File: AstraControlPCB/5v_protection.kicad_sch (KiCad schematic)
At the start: 9 parts, among them U2 NCP361SNT1G

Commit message: Updates
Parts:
- renumbered R14 to R8, R8 to R9
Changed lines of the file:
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@@
 			)
 		)
-		(property "Datasheet" ""
+		(property "Datasheet" "https://www.lcsc.com/product-detail/Thimble-Copper-Rod-Test-Ring_ronghe-RH-5000_C5277086.html"
 			(at 177.8 119.38 90)
 			(effects
@@
 		(dnp no)
 		(fields_autoplaced yes)
-		(property "Reference" "R14"
+		(property "Reference" "R8"
 			(at 116.84 100.33 0)
 			(effects
@@
 			(project "AstraControl"
 				(path "/9a751838-dce8-4d69-8a02-736625ac74e7/0db21d8e-3390-4d67-877f-0e5d98e37848/e21714b4-6921-40f8-8882-480f43314016"
-					(reference "R14")
+					(reference "R8")
 					(unit 1)
 				)
@@
 		(dnp no)
 		(fields_autoplaced yes)
-		(property "Reference" "R8"
+		(property "Reference" "R9"
 			(at 241.3 90.17 0)
 			(effects
@@
 			(project "AstraControl"
 				(path "/9a751838-dce8-4d69-8a02-736625ac74e7/0db21d8e-3390-4d67-877f-0e5d98e37848/e21714b4-6921-40f8-8882-480f43314016"
-					(reference "R8")
+					(reference "R9")
 					(unit 1)
 				)
@@
 			)
 		)
-		(property "Datasheet" ""
+		(property "Datasheet" "https://www.lcsc.com/product-detail/Thimble-Copper-Rod-Test-Ring_ronghe-RH-5000_C5277086.html"
 			(at 114.3 76.2 90)
 			(effects

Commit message: Added MFN MPR to each components for eurocircuits
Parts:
- C7, C8: MFN (none) -> Samsung Electro-Mechanics; MPR (none) -> CL05A105KA5NQNC
- LED2: MFN (none) -> Hubei KENTO Elec; MPN (none) -> KT-0603R
- R8: MFN (none) -> UNI-ROYAL(Uniroyal Elec); MPN (none) -> 0805W8F1004T5E
- R9: MFN (none) -> UNI-ROYAL(Uniroyal Elec); MPN (none) -> 0402WGF2200TCE
- TP5, TP6: MFN (none) -> ronghe; MPN (none) -> RH-5000
- U2: MFN (none) -> onsemi; MPN (none) -> NCP361SNT1G
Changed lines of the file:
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@@
 			)
 		)
-		(property "Description" "Multilayer Ceramic Capacitor"
+		(property "Description" "25V 1uF X5R ±10% 0402 Multilayer Ceramic Capacitors MLCC - SMD/SMT ROHS"
 			(at 132.08 91.44 0)
 			(effects
@@
 				)
 				(justify right)
+			)
+		)
+		(property "MFN" "Samsung Electro-Mechanics"
+			(at 151.13 91.44 0)
+			(effects
+				(font
+					(size 1.27 1.27)
+				)
+				(hide yes)
+			)
+		)
+		(property "MPR" "CL05A105KA5NQNC"
+			(at 147.32 91.44 0)
+			(effects
+				(font
+					(size 1.27 1.27)
+				)
+				(hide yes)
 			)
 		)
@@
 			)
 		)
-		(property "Description" "0603 Smd LED Emitting Color Red"
+		(property "Description" "-40℃~+85℃ Red 0603 LED Indication - Discrete ROHS"
 			(at 208.28 104.14 0)
 			(effects
@@
 					(bold yes)
 				)
+			)
+		)
+		(property "MFN" "Hubei KENTO Elec"
+			(at 208.28 123.19 0)
+			(effects
+				(font
+					(size 1.27 1.27)
+				)
+				(hide yes)
+			)
+		)
+		(property "MPN" "KT-0603R"
+			(at 208.28 123.19 0)
+			(effects
+				(font
+					(size 1.27 1.27)
+				)
+				(hide yes)
 			)
 		)
@@
 			)
 		)
-		(property "Description" ""
+		(property "Description" "Test Points / Test Rings ROHS"
 			(at 177.8 119.38 90)
 			(effects
@@
 				)
 				(justify left)
+			)
+		)
+		(property "MFN" "ronghe"
+			(at 177.8 153.67 0)
+			(effects
+				(font
+					(size 1.27 1.27)
+				)
+				(hide yes)
+			)
+		)
+		(property "MPN" "RH-5000"
+			(at 177.8 153.67 0)
+			(effects
+				(font
+					(size 1.27 1.27)
+				)
+				(hide yes)
 			)
 		)
@@
 			)
 		)
-		(property "Description" "Chip Resistor - Surface Mount ROHS"
+		(property "Description" "125mW Thick Film Resistors 150V ±100ppm/℃ ±1% 1MΩ 0805 Chip Resistor - Surface Mount ROHS"
 			(at 116.84 104.14 0)
 			(effects
@@
 					(bold yes)
 				)
+			)
+		)
+		(property "MFN" "UNI-ROYAL(Uniroyal Elec)"
+			(at 116.84 88.9 0)
+			(effects
+				(font
+					(size 1.27 1.27)
+				)
+				(hide yes)
+			)
+		)
+		(property "MPN" "0805W8F1004T5E"
+			(at 116.84 88.9 0)
+			(effects
+				(font
+					(size 1.27 1.27)
+				)
+				(hide yes)
 			)
 		)
@@
 			)
 		)
-		(property "Description" "Thick Film Resistors"
+		(property "Description" "62.5mW Thick Film Resistors 50V ±100ppm/℃ ±1% 220Ω 0402 Chip Resistor - Surface Mount ROHS"
 			(at 241.3 93.98 0)
 			(effects
@@
 					(bold yes)
 				)
+			)
+		)
+		(property "MFN" "UNI-ROYAL(Uniroyal Elec)"
+			(at 241.3 78.74 0)
+			(effects
+				(font
+					(size 1.27 1.27)
+				)
+				(hide yes)
+			)
+		)
+		(property "MPN" "0402WGF2200TCE"
+			(at 241.3 78.74 0)
+			(effects
+				(font
+					(size 1.27 1.27)
+				)
+				(hide yes)
 			)
 		)
@@
 			)
 		)
+		(property "MFN" "onsemi"
+			(at 152.4 157.48 0)
+			(effects
+				(font
+					(size 1.27 1.27)
+				)
+				(hide yes)
+			)
+		)
+		(property "MPN" "NCP361SNT1G"
+			(at 152.4 157.48 0)
+			(effects
+				(font
+					(size 1.27 1.27)
+				)
+				(hide yes)
+			)
+		)
 		(pin "2"
 		)
@@
 			)
 		)
-		(property "Description" "Multilayer Ceramic Capacitor"
+		(property "Description" "25V 1uF X5R ±10% 0402 Multilayer Ceramic Capacitors MLCC - SMD/SMT ROHS"
 			(at 165.1 91.44 0)
 			(effects
@@
 				)
 				(justify left)
+			)
+		)
+		(property "MFN" "Samsung Electro-Mechanics"
+			(at 146.05 91.44 0)
+			(effects
+				(font
+					(size 1.27 1.27)
+				)
+				(hide yes)
+			)
+		)
+		(property "MPR" "CL05A105KA5NQNC"
+			(at 149.86 91.44 0)
+			(effects
+				(font
+					(size 1.27 1.27)
+				)
+				(hide yes)
 			)
 		)
@@
 			)
 		)
-		(property "Description" ""
+		(property "Description" "Test Points / Test Rings ROHS"
 			(at 114.3 76.2 90)
 			(effects
@@
 			)
 		)
+		(property "MFN" "ronghe"
+			(at 114.3 110.49 0)
+			(effects
+				(font
+					(size 1.27 1.27)
+				)
+				(hide yes)
+			)
+		)
+		(property "MPN" "RH-5000"
+			(at 114.3 110.49 0)
+			(effects
+				(font
+					(size 1.27 1.27)
+				)
+				(hide yes)
+			)
+		)

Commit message: Migrate library to submodule
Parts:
- C7, C8: MPN (none) -> CL05A105KA5NQNC
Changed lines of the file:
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@@
+			)
+		)
+		(property "MPN" "CL05A105KA5NQNC"
+			(at 147.32 91.44 0)
+			(effects
+				(font
+					(size 1.27 1.27)
+				)
+				(hide yes)
 			)
 		)
@@
 			(at 149.86 91.44 0)
 			(effects
+				(font
+					(size 1.27 1.27)
+				)
+				(hide yes)
+			)
+		)
+		(property "MPN" "CL05A105KA5NQNC"
+			(at 149.86 91.44 0)
+			(effects

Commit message: Update schematic titles, templates
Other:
- title: AstraControl - Root -> AstraControl - 5V Protection
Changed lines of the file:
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@@
 	(paper "A4")
 	(title_block
-		(title "AstraControl - Root")
+		(title "AstraControl - 5V Protection")
 		(date "2024-08-26")
 		(rev "A")

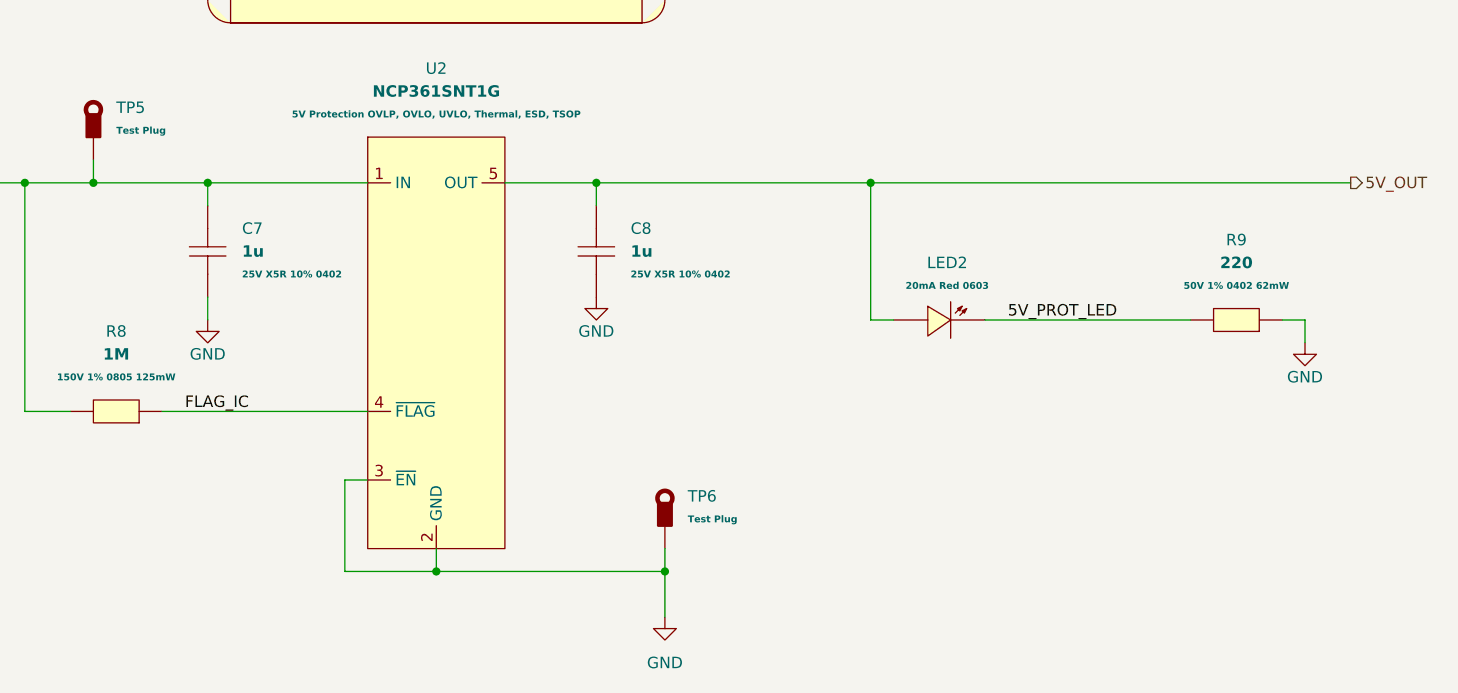
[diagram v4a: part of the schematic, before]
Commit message: Update to new rs485 chip, use 2 bit 5v gpio
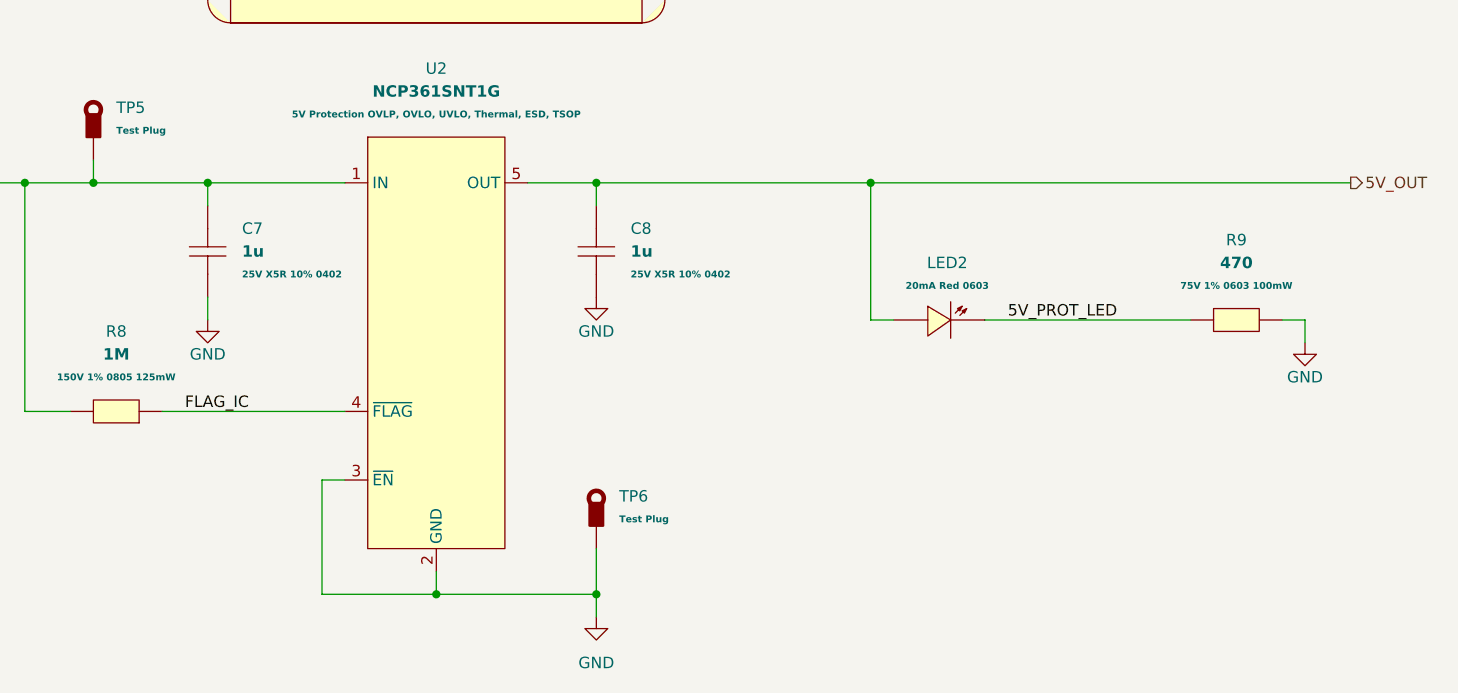
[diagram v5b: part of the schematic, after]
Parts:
- removed R9: 220, LiveAstra:R_0402_1005Metric, symbol LiveAstra:R_220Ohm_0402_62mW
- added R9: 470, LiveAstra:R_0603_1608Metric, symbol LiveAstra:R_470Ohm_0603_100mW
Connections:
- net 5V_PROT_LED: now also R9.1
- net GND: now also R9.2
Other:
- moved on the sheet: TP6, U2

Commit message: New inductor that is in stock, updated rs485 ic layout to put caps closer
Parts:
- renumbered INF3 to INF4, R9 to R10, R8 to R9
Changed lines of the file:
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@@
 		(dnp no)
 		(fields_autoplaced yes)
-		(property "Reference" "R9"
+		(property "Reference" "R10"
 			(at 241.3 90.17 0)
 			(effects
@@
 			(project ""
 				(path "/9a751838-dce8-4d69-8a02-736625ac74e7/0db21d8e-3390-4d67-877f-0e5d98e37848/e21714b4-6921-40f8-8882-480f43314016"
-					(reference "R9")
+					(reference "R10")
 					(unit 1)
 				)
@@
 		(on_board yes)
 		(dnp no)
-		(property "Reference" "#PWR020"
+		(property "Reference" "#PWR021"
 			(at 248.92 107.95 0)
 			(effects
@@
 			(project "AstraControl"
 				(path "/9a751838-dce8-4d69-8a02-736625ac74e7/0db21d8e-3390-4d67-877f-0e5d98e37848/e21714b4-6921-40f8-8882-480f43314016"
-					(reference "#PWR020")
+					(reference "#PWR021")
 					(unit 1)
 				)
@@
 		(dnp no)
 		(fields_autoplaced yes)
-		(property "Reference" "#PWR019"
+		(property "Reference" "#PWR020"
 			(at 170.18 138.43 0)
 			(effects
@@
 			(project "AstraControl"
 				(path "/9a751838-dce8-4d69-8a02-736625ac74e7/0db21d8e-3390-4d67-877f-0e5d98e37848/e21714b4-6921-40f8-8882-480f43314016"
-					(reference "#PWR019")
+					(reference "#PWR020")
 					(unit 1)
 				)
@@
 		(dnp no)
 		(fields_autoplaced yes)
-		(property "Reference" "R8"
+		(property "Reference" "R9"
 			(at 116.84 100.33 0)
 			(effects
@@
 			(project "AstraControl"
 				(path "/9a751838-dce8-4d69-8a02-736625ac74e7/0db21d8e-3390-4d67-877f-0e5d98e37848/e21714b4-6921-40f8-8882-480f43314016"
-					(reference "R8")
+					(reference "R9")
 					(unit 1)
 				)
@@
 		(on_board yes)
 		(dnp no)
-		(property "Reference" "#PWR018"
+		(property "Reference" "#PWR019"
 			(at 170.18 102.87 0)
 			(effects
@@
 			(project "AstraControl"
 				(path "/9a751838-dce8-4d69-8a02-736625ac74e7/0db21d8e-3390-4d67-877f-0e5d98e37848/e21714b4-6921-40f8-8882-480f43314016"
-					(reference "#PWR018")
+					(reference "#PWR019")
 					(unit 1)
 				)
@@
 		(on_board yes)
 		(dnp no)
-		(property "Reference" "#PWR017"
+		(property "Reference" "#PWR018"
 			(at 127 105.41 0)
 			(effects
@@
 			(project "AstraControl"
 				(path "/9a751838-dce8-4d69-8a02-736625ac74e7/0db21d8e-3390-4d67-877f-0e5d98e37848/e21714b4-6921-40f8-8882-480f43314016"
-					(reference "#PWR017")
+					(reference "#PWR018")
 					(unit 1)
 				)
@@
 		(on_board no)
 		(dnp no)
-		(property "Reference" "INF3"
+		(property "Reference" "INF4"
 			(at 149.86 43.18 0)
 			(effects
@@
 			(project ""
 				(path "/9a751838-dce8-4d69-8a02-736625ac74e7/0db21d8e-3390-4d67-877f-0e5d98e37848/e21714b4-6921-40f8-8882-480f43314016"
-					(reference "INF3")
-					(unit 1)
-				)
+					(reference "INF4")
+					(unit 1)
+				)

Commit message: Update revision and add year to silkscreen
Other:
- title: AstraControl - 5V Protection -> AstraControl - Root
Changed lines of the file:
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@@
 	(paper "A4")
 	(title_block
-		(title "AstraControl - 5V Protection")
+		(title "AstraControl - Root")
 		(date "2024-08-26")
-		(rev "A")
+		(rev "B")
 		(company "LiveAstra Technologies")
 	)

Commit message: Updated resistors for leds, added more back silkscreen
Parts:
- removed R10: 470, LiveAstra:R_0603_1608Metric, symbol LiveAstra:R_470Ohm_0603_100mW
- added R10: 1k, LiveAstra:R_0603_1608Metric, symbol LiveAstra:R_1kOhm_0603_100mW
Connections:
- net 5V_PROT_LED: now also R10.1
- net GND: now also R10.2
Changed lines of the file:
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@@
-	)
-	(symbol
-		(lib_id "LiveAstra:R_470Ohm_0603_100mW")
-		(at 241.3 99.06 0)
-		(unit 1)
-		(exclude_from_sim no)
-		(in_bom yes)
-		(on_board yes)
-		(dnp no)
-		(fields_autoplaced yes)
-		(property "Reference" "R10"
-			(at 241.3 90.17 0)
-			(effects
-				(font
-					(size 1.27 1.27)
-				)
-			)
-		)
-		(property "Value" "470"
-			(at 241.3 92.71 0)
-			(effects
-				(font
-					(size 1.27 1.27)
-					(bold yes)
-				)
-			)
-		)
-		(property "Footprint" "LiveAstra:R_0603_1608Metric"
-			(at 241.3 104.14 0)
-			(effects
-				(font
-					(size 1.27 1.27)
-				)
-				(hide yes)
-			)
-		)
-		(property "Datasheet" "https://lcsc.com/product-detail/Chip-Resistor-Surface-Mount-UniOhm_470R-4700-1_C23179.html"
-			(at 241.3 106.68 0)
-			(effects
-				(font
-					(size 1.27 1.27)
-				)
-				(hide yes)
-			)
-		)
-		(property "Description" "100mW Thick Film Resistors 75V ±100ppm/℃ ±1% 470Ω 0603 Chip Resistor - Surface Mount ROHS"
-			(at 241.3 111.76 0)
-			(effects
-				(font
-					(size 1.27 1.27)
-				)
-				(hide yes)
-			)
-		)
-		(property "LCSC Part" "C23179"
-			(at 241.3 109.22 0)
-			(effects
-				(font
-					(size 1.27 1.27)
-				)
-				(hide yes)
-			)
-		)
-		(property "Extra Values" "75V 1% 0603 100mW"
-			(at 241.3 95.25 0)
-			(effects
-				(font
-					(size 0.762 0.762)
-					(bold yes)
-				)
-			)
-		)
-		(property "MFN" "UNI-ROYAL(Uniroyal Elec)"
-			(at 241.3 116.84 0)
-			(effects
-				(font
-					(size 1.27 1.27)
-				)
-				(hide yes)
-			)
-		)
-		(property "MPN" "0603WAF4700T5E"
-			(at 242.57 114.3 0)
-			(effects
-				(font
-					(size 1.27 1.27)
-				)
-				(hide yes)
-			)
-		)
-		(pin "2"
-		)
-		(pin "1"
-		)
-		(instances
-			(project ""
-				(path "/9a751838-dce8-4d69-8a02-736625ac74e7/0db21d8e-3390-4d67-877f-0e5d98e37848/e21714b4-6921-40f8-8882-480f43314016"
-					(reference "R10")
-					(unit 1)
-				)
-			)
-		)
 	)
 	(symbol
@@
 					(unit 1)
 				)
+			)
+		)
+	)
+	(symbol
+		(lib_id "LiveAstra:R_1kOhm_0603_100mW")
+		(at 241.3 99.06 0)
+		(unit 1)
+		(exclude_from_sim no)
+		(in_bom yes)
+		(on_board yes)
+		(dnp no)
+		(fields_autoplaced yes)
+		(property "Reference" "R10"
+			(at 241.3 90.17 0)
+			(effects
+				(font
+					(size 1.27 1.27)
+				)
+			)
+		)
+		(property "Value" "1k"
+			(at 241.3 92.71 0)
+			(effects
+				(font
+					(size 1.27 1.27)
+					(bold yes)
+				)
+			)
+		)
+		(property "Footprint" "LiveAstra:R_0603_1608Metric"
+			(at 241.3 107.95 0)
+			(effects
+				(font
+					(size 1.27 1.27)
+				)
+				(hide yes)
+			)
+		)
+		(property "Datasheet" "https://www.lcsc.com/product-detail/Chip-Resistor-Surface-Mount_UNI-ROYAL-Uniroyal-Elec-0603WAJ0102T5E_C25585.html"
+			(at 241.3 111.76 0)
+			(effects
+				(font
+					(size 1.27 1.27)
+				)
+				(hide yes)
+			)
+		)
+		(property "Description" "100mW Thick Film Resistors 75V ±100ppm/℃ ±5% 1kΩ 0603 Chip Resistor - Surface Mount ROHS"
+			(at 241.3 104.14 0)
+			(effects
+				(font
+					(size 1.27 1.27)
+				)
+				(hide yes)
+			)
+		)
+		(property "LCSC Part" "C25585"
+			(at 241.3 115.57 0)
+			(effects
+				(font
+					(size 1.27 1.27)
+				)
+				(hide yes)
+			)
+		)
+		(property "Extra Values" "75V 1% 0603 100mW "
+			(at 241.3 95.25 0)
+			(effects
+				(font
+					(size 0.762 0.762)
+					(bold yes)
+				)
+			)
+		)
+		(property "MPN" "0603WAJ0102T5E"
+			(at 241.3 119.38 0)
+			(effects
+				(font
+					(size 1.27 1.27)
+				)
+				(hide yes)
+			)
+		)
+		(property "MFN" "UNI-ROYAL(Uniroyal Elec)"
+			(at 241.3 123.19 0)
+			(effects
+				(font
+					(size 1.27 1.27)
+				)
+				(hide yes)
+			)
+		)
+		(pin "2"
+		)
+		(pin "1"
+		)
+		(instances
+			(project ""
+				(path "/9a751838-dce8-4d69-8a02-736625ac74e7/0db21d8e-3390-4d67-877f-0e5d98e37848/e21714b4-6921-40f8-8882-480f43314016"
+					(reference "R10")
+					(unit 1)
+				)
